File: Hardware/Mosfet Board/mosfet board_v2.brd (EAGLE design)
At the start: 50 x 29.2 mm, 26 parts, among them IC1 4081D, U1 MOSFET1, U2 MOSFET2, U3 MOSFET3

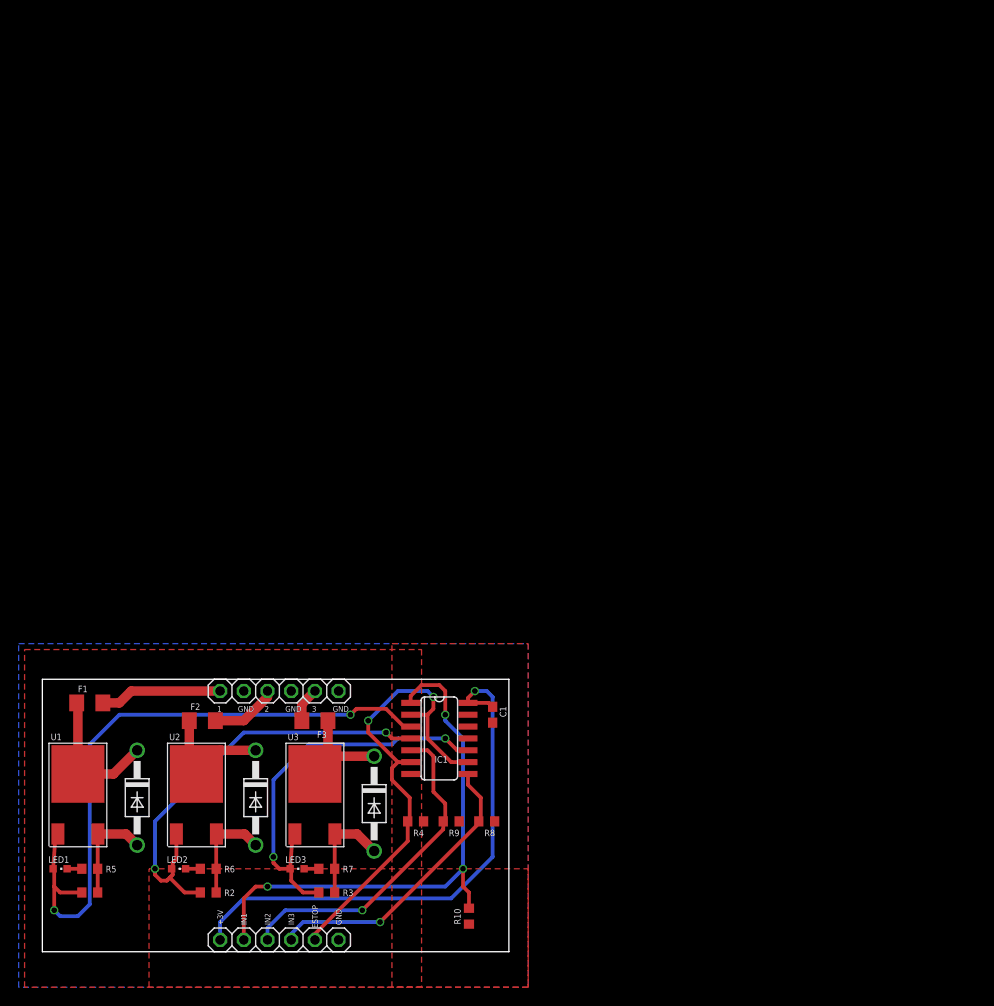
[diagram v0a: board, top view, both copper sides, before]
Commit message: new independent mosfet board
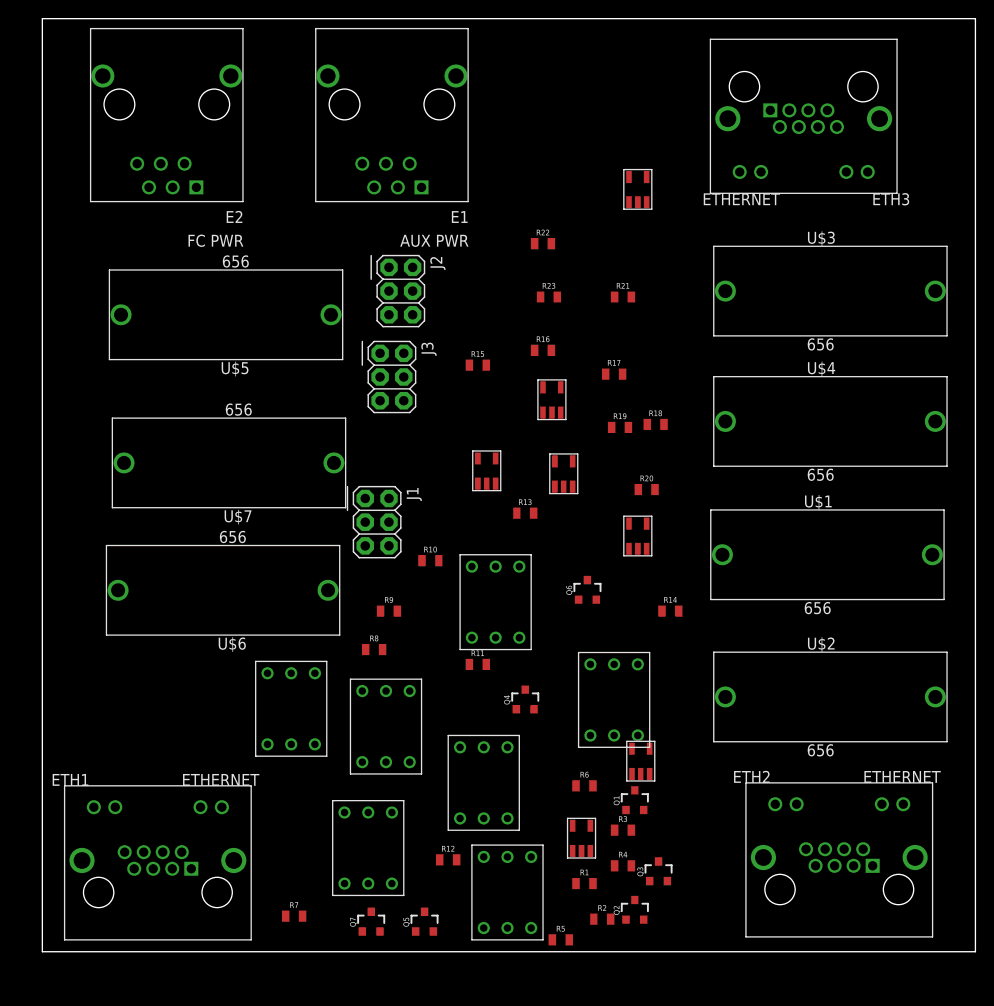
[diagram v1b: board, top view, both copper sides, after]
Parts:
- removed C1: (no value), E-P-008-R1.2:C0603
- removed D1: D1, diode:DO41-10
- removed D2: D2, diode:DO41-10
- removed D3: D3, diode:DO41-10
- removed F1, F2, F3: (no value), polyfuse:1206
- removed IC1: 4081D, 40xx:SO14
- removed JP1, JP2: (no value), adafruit:1X06
- removed LED1, LED2, LED3: (no value), adafruit:CHIPLED_0603
- removed U1: MOSFET1, MOSFET:MOSFET
- removed U2: MOSFET2, MOSFET:MOSFET
- removed U3: MOSFET3, MOSFET:MOSFET
- added E1: AUX PWR, 5555140-6 RJ11:1734723-1_RJ11
- added E2: FC PWR, 5555140-6 RJ11:1734723-1_RJ11
- added ETH1, ETH2, ETH3: ETHERNET, ETHERNET:A122645-ND
- added FRAME1, FRAME2: FRAME-LETTERNO_PACKAGE, FRAME-LETTER:DUMMY
- added J1, J2, J3: (no value), SparkFun-Connectors:2X03
- added Q1, Q2, Q3, Q4, Q5, Q6, Q7: (no value), n-mos switch:SOT23-3
- added R11, R13, R18, R20: 10k, Resistor:0805
- added R12, R14, R19, R21: 100, Resistor:0805
- added R15, R16, R17, R22, R23: 1k, Resistor:0805
- added U$1, U$2, U$3, U$4, U$5, U$6, U$7: 656, GlassFuseHolder:656
- added U$10, U$12, U$14, U$16, U$18, U$20, U$8: H11L1M, H11L1M:H11L1M
- added U$11, U$13, U$15, U$17, U$19, U$21, U$9: SN74LVC1G04-Q1, SN74LVC1G04-Q1:SOT-23-5
- R1: value R1 -> 100; device resistor:R0603 -> Resistor:0805
- R10: value 10k -> 1k; device adafruit:R0603 -> Resistor:0805
- R2: value R2 -> 10k; device resistor:R0603 -> Resistor:0805
- R3: value R3 -> 10k; device resistor:R0603 -> Resistor:0805
- R4, R8: value 10k -> 100; device adafruit:R0603 -> Resistor:0805
- R5, R6: value 1k -> 10k; device resistor:R0603 -> Resistor:0805
- R7: device resistor:R0603 -> Resistor:0805
- R9: device adafruit:R0603 -> Resistor:0805
- moved R1 53.0 mm to (58.1, 7.30), turned to 0 degrees
- moved R5 51.1 mm to (55.6, 1.27), turned to 0 degrees
- moved R2 42.3 mm to (60.0, 3.49), turned to 0 degrees
- moved R6 41.3 mm to (58.1, 17.8), turned to 0 degrees
- moved R10 38.3 mm to (41.6, 41.9), turned to 0 degrees
- moved R3 32.4 mm to (62.2, 13.0), turned to 0 degrees
- moved R9 23.5 mm to (37.1, 36.5), turned to 0 degrees
- moved R4 22.7 mm to (62.2, 9.21), turned to 0 degrees
- moved R8 22.0 mm to (35.6, 32.4), turned to 0 degrees
- moved R7 6.16 mm to (27.0, 3.81), turned to 0 degrees
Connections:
- removed net ESTOP: IC1.2, IC1.6, IC1.9, JP2.5, R4.2
- removed net IN1: IC1.1, JP2.2, R10.2
- removed net IN2: IC1.5, JP2.3, R9.2
- removed net IN3: IC1.8, JP2.4, R8.2
- removed net OUT1: D1.C, F1.1, U1.P$2
- removed net OUT2: D2.C, F2.1, U2.P$2
- removed net OUT3: D3.C, F3.1, U3.P$2
- removed net VDD: C1.1, IC1.14, JP2.1
- removed net VSS: C1.2, IC1.7, JP2.6, R10.1, R4.1, R8.1, R9.1
- new net 1_H: J1.1, U$1.P$1
- new net 1_L: ETH2.P$1, Q1.3
- new net 2_H: J1.3, U$2.P$1
- new net 2_L: ETH2.P$3, Q2.3
- new net 3_H: J1.5, U$3.P$1
- new net 3_L: ETH2.P$5, Q3.3
- new net 4_H: J2.1, U$4.P$1
- new net 4_L: ETH2.P$7, Q4.3
- new net 5_H: J2.3, U$5.P$1
- new net 5_L: ETH1.P$1, Q5.3
- new net 6_H: J2.5, U$6.P$1
- new net 6_L: ETH1.P$3, Q6.3
- new net 7_H: J3.1, U$7.P$1
- new net 7_L: ETH1.P$5, Q7.3
- new net AUX_12V: E1.3, E1.4, J1.4, J2.2, J2.6, J3.4
- new net AUX_5V: E1.2, E1.5, J3.3
- new net FC_12V: E2.3, E2.4, J1.2, J1.6, J2.4, J3.2, J3.6
- new net FC_5V: E2.2, E2.5, J3.5, R3.1, R6.1, U$10.P$6, U$11.P$5, U$12.P$6, U$13.P$5, U$14.P$6, U$15.P$5, U$16.P$6, U$17.P$5, U$18.P$6, U$19.P$5, U$20.P$6, U$21.P$5, U$8.P$6, U$9.P$5
- new net GND_ISOLATED: ETH3.P$8, U$10.P$2, U$12.P$2, U$14.P$2, U$16.P$2, U$18.P$2, U$20.P$2, U$8.P$2
- new net IN_1: ETH3.P$1, R7.2
- new net IN_2: ETH3.P$2, R10.2
- new net IN_3: ETH3.P$3, R17.2
- new net IN_4: ETH3.P$4, R16.2
- new net IN_5: ETH3.P$5, R15.2
- new net IN_6: ETH3.P$6, R22.2
- new net IN_7: ETH3.P$7, R23.2
- new net N$13: Q3.1, R8.2, R9.2
- new net N$14: Q4.1, R11.2, R12.2
- new net N$15: Q5.1, R14.2
- new net N$16: Q6.1, R18.2, R19.2
- new net N$17: R6.2, U$10.P$4, U$11.P$2
- new net N$18: R4.2, U$11.P$4
- new net N$19: Q7.1, R20.2, R21.2
- new net N$20: R17.1, U$12.P$1
- new net N$21: R16.1, U$14.P$1
- new net N$22: R15.1, U$16.P$1
- new net N$23: R22.1, U$18.P$1
- new net N$24: R23.1, U$20.P$1
- new net N$25: R10.1, U$10.P$1
- new net N$26: R7.1, U$8.P$1
- new net N$29: U$12.P$4, U$13.P$2
- new net N$3: ETH2.P$4, U$2.P$2
- new net N$30: R8.1, U$13.P$4
- new net N$38: U$16.P$4, U$17.P$2
- new net N$41: R14.1, U$17.P$4
- new net N$46: U$14.P$4, U$15.P$2
- new net N$47: R12.1, U$15.P$4
- new net N$5: ETH2.P$8, U$4.P$2
- new net N$54: U$20.P$4, U$21.P$2
- new net N$59: R21.1, U$21.P$4
- new net N$64: U$18.P$4, U$19.P$2
- new net N$67: R19.1, U$19.P$4
- net GND: now also E1.1, E1.6, E1.SH1, E1.SH2, E2.1, E2.6, E2.SH1, E2.SH2, ETH1.P$13, ETH1.P$14, ETH2.P$13, ETH2.P$14, ETH3.P$13, ETH3.P$14, Q1.2, Q2.2, Q3.2, Q4.2, Q5.2, Q6.2, Q7.2, R11.1, R13.1, R18.1, R2.2, R20.1, R5.2, R9.1, U$10.P$5, U$11.P$1, U$11.P$3, U$12.P$5, U$13.P$1, U$13.P$3, U$14.P$5, U$15.P$1, U$15.P$3, U$16.P$5, U$17.P$1, U$17.P$3, U$18.P$5, U$19.P$1, U$19.P$3, U$20.P$5, U$21.P$1, U$21.P$3, U$8.P$5, U$9.P$1, U$9.P$3; no longer D1.A, D2.A, D3.A, JP1.2, JP1.4, JP1.6, R1.1, R2.1, R3.1, R5.1, R6.1, R7.1, U1.P$3, U2.P$3, U3.P$3
- net N$1: now also ETH2.P$2, U$1.P$2; no longer IC1.3, LED1.A, R1.2, U1.P$1
- net N$10: now also ETH1.P$6, U$7.P$2; no longer LED1.C, R5.2
- net N$11: now also ETH1.P$4, U$6.P$2; no longer LED2.C, R6.2
- net N$12: now also Q2.1, R4.1, R5.1; no longer LED3.C, R7.2
- net N$4: now also ETH2.P$6, U$3.P$2; no longer IC1.4, LED2.A, R2.2, U2.P$1
- net N$6: now also ETH1.P$2, U$5.P$2; no longer IC1.10, LED3.A, R3.2, U3.P$1
- net N$7: now also Q1.1, R1.1, R2.1; no longer F1.2, JP1.1
- net N$8: now also R3.2, U$8.P$4, U$9.P$2; no longer F2.2, JP1.3
- net N$9: now also R1.2, U$9.P$4; no longer F3.2, JP1.5
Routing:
- net N$1: track 70.1 -> 0.00 mm, vias 2 -> 0
- net IN1: track 58.8 -> 0.00 mm, vias 3 -> 0
- net VDD: track 57.7 -> 0.00 mm, vias 1 -> 0
- net ESTOP: track 51.9 -> 0.00 mm, vias 2 -> 0
- net N$4: track 48.3 -> 0.00 mm, vias 2 -> 0
- net N$6: track 42.8 -> 0.00 mm, vias 2 -> 0
- net IN2: track 35.6 -> 0.00 mm, vias 1 -> 0
- net GND: track 33.2 -> 0.00 mm
- net IN3: track 31.6 -> 0.00 mm, vias 1 -> 0
- net OUT1: track 15.1 -> 0.00 mm
- net OUT3: track 14.7 -> 0.00 mm
- net OUT2: track 13.4 -> 0.00 mm
- net N$7: track 13.1 -> 0.00 mm
- net N$8: track 7.27 -> 0.00 mm
- net N$9: track 3.75 -> 0.00 mm
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- removed copper zone on layer 1, net GND
- removed copper zone on layer 16, net GND
- removed copper zone on layer 1, net VSS
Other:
- board size 50 x 29.2 mm -> 100 x 100 mm
- board text removed: "+3V"
- board text removed: "1"
- board text removed: "2"
- board text removed: "3"
- board text removed: "ESTOP"
- board text removed: "GND"
- board text removed: "IN1"
- board text removed: "IN2"
- board text removed: "IN3"
